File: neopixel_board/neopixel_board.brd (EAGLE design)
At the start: 160 x 100 mm, 63 parts, among them U1 UA7805CKCT, U2 MIC5219, U3 ATMEGA32U4, U4 UA7805CKCT, U5 UA7805CKCT, U6 UA7805CKCT, Y1 16MHz

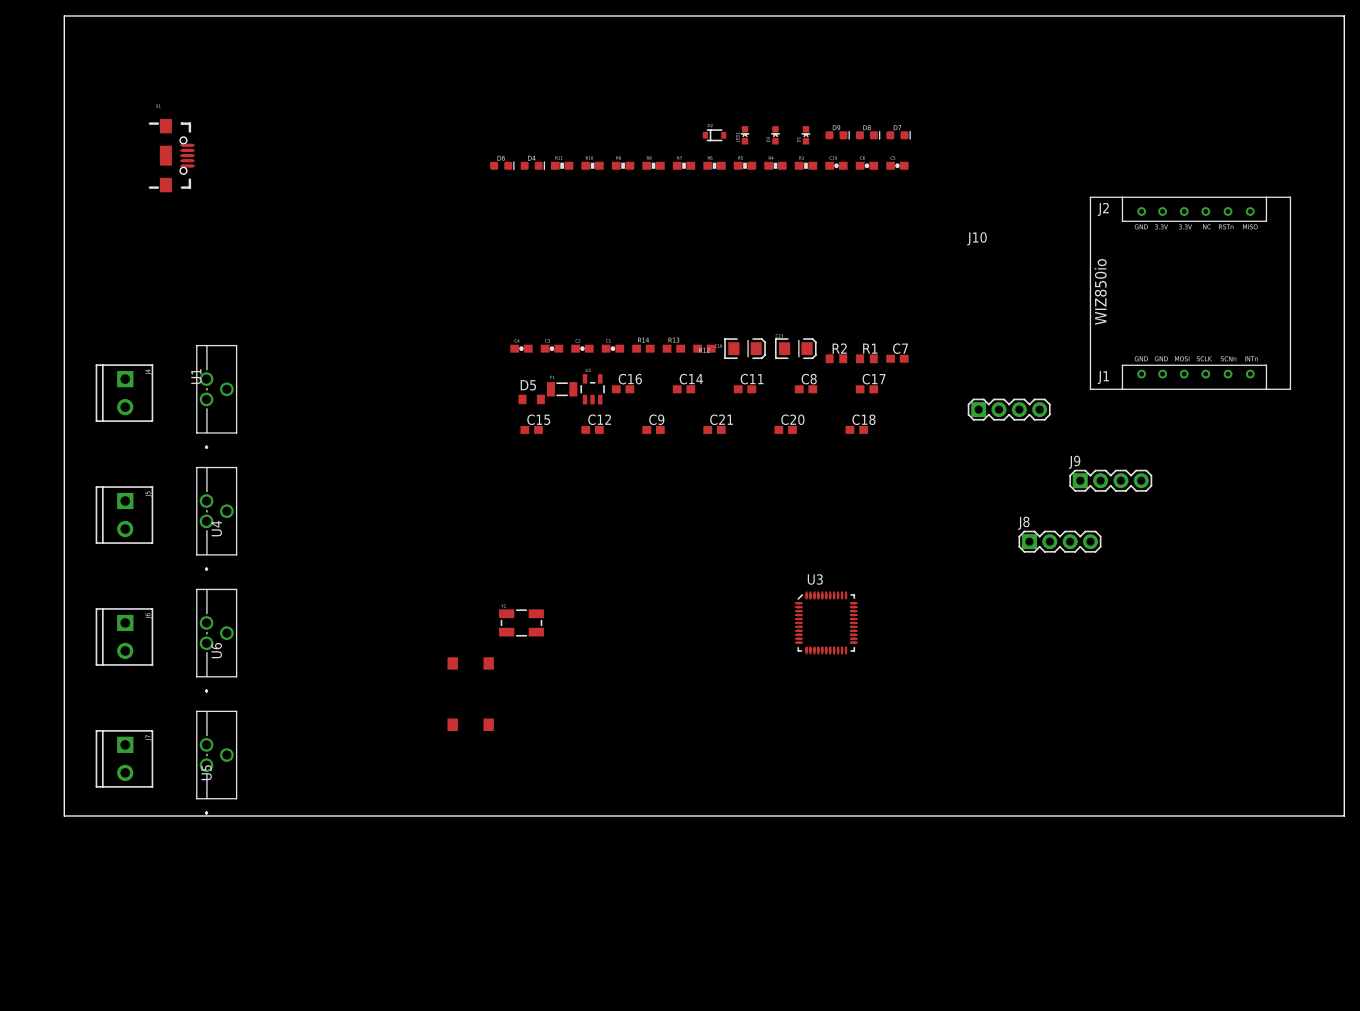
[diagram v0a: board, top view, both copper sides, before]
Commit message: SCH fixes and BRD WIP
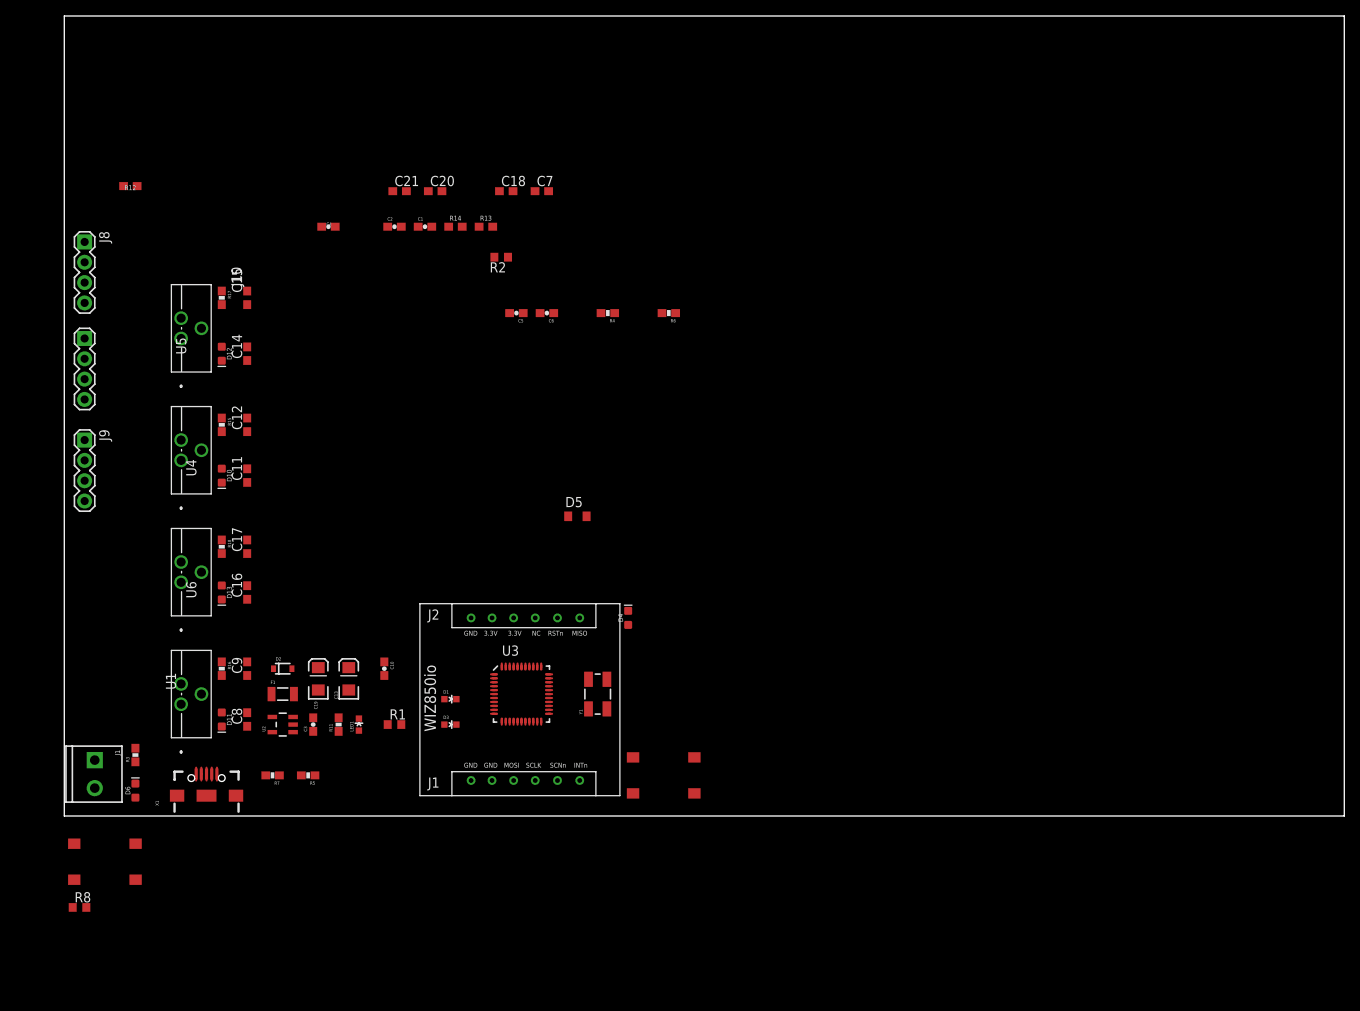
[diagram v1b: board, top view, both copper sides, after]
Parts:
- removed D7, D8, D9: GREEN, SparkFun-LED:LED-0603
- removed J4, J5, J6, J7: (no value), SparkFun-Connectors:SCREWTERMINAL-3.5MM-2
- removed R10, R9: 1K, SparkFun:0603-RES
- added D10, D11, D12, D13: GREEN, SparkFun-LED:LED-0603
- added J1: (no value), SparkFun-Connectors:SCREWTERMINAL-3.5MM-2
- added PB2: PTS645PTS645_SMD1, Training_Board:PTS645_SMD
- added R15, R16, R17, R18: 1K, SparkFun:0603-RES
- R8: value 1K -> (none); device SparkFun:0603-RES -> rcl:R0603
- moved J9 124.6 mm to (2.54, 47.0), turned to 270 degrees
- moved J8 123.9 mm to (2.54, 71.8), turned to 270 degrees
- moved R8 117.2 mm to (1.91, -11.4)
- moved J10 112.1 mm to (2.54, 59.7), turned to 270 degrees
- moved R3 111.6 mm to (8.89, 7.62), turned to 90 degrees
- moved ETH1 98.0 mm to (44.5, 2.54)
- moved R5 93.7 mm to (30.5, 5.08), turned to 180 degrees
- moved R7 91.9 mm to (26.0, 5.08), turned to 180 degrees
- moved D6 90.5 mm to (8.89, 3.17), turned to 90 degrees
- moved LED1 88.1 mm to (36.8, 11.4)
- moved D2 85.8 mm to (27.3, 18.4)
- moved C10 84.5 mm to (40.0, 18.4), turned to 270 degrees
- moved D3 84.1 mm to (48.3, 11.4), turned to 270 degrees
- moved D1 83.3 mm to (48.3, 14.6), turned to 270 degrees
- moved C8 81.1 mm to (22.9, 12.1), turned to 90 degrees
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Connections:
- net MISO renamed ETH_MISO
- net MOSI renamed ETH_MOSI
- removed net A0: U3.36
- removed net A1: U3.37
- removed net A2: U3.38
- removed net A3: U3.39
- removed net A4: U3.40
- removed net A5: U3.41
- removed net D11: U3.12
- removed net D12: U3.26
- removed net D13: U3.32
- removed net D2: U3.19
- removed net D3: U3.18
- removed net D4: U3.25
- removed net D6: U3.27
- removed net D7: U3.1
- removed net D8: U3.28
- removed net N$3: D5.C
- removed net PB5: R13.2
- removed net PB6: R14.2
- removed net PC6: R12.2
- removed net RXI: U3.20
- removed net TXO: U3.21
- removed net VSOURCE1: C8.1, J4.2, R8.2, U1.1
- removed net VSOURCE2: C11.1, J5.2, R3.2, U4.1
- removed net VSOURCE3: C14.1, J6.2, R9.2, U5.1
- removed net VSOURCE4: C16.1, J7.2, R10.2, U6.1
- new net ETH_RST: PB2.P$1, PB2.P$2, R8.2, U3.20
- new net N$21: D6.A, R3.1
- new net VSOURCE: C11.1, C14.1, C16.1, C8.1, J1.2, R3.2, U1.1, U4.1, U5.1, U6.1
- net D10: now also R14.2
- net D5: now also R12.2
- net D9: now also R13.2
- net GND: now also D10.C, D11.C, D12.C, D13.C, J1.1, PB2.P$3, PB2.P$4; no longer D7.C, D8.C, D9.C, J4.1, J5.1, J6.1, J7.1
- net N$10: now also D13.A, R18.2; no longer D7.A, R3.1
- net N$11: now also D11.A, R16.2; no longer D9.A, R10.1
- net N$12: now also D10.A, R15.2; no longer D8.A, R9.1
- net N$13: now also D12.A, R17.2; no longer D6.A, R8.1
- net RAW: now also D5.C
- net VCC1: now also R16.1
- net VCC1_3.3V: now also R8.1
- net VCC2: now also R15.1
- net VCC3: now also R17.1
- net VCC4: now also R18.1

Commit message: SCH finish BRD WIP
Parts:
- removed D13: GREEN, SparkFun-LED:LED-0603
- removed R16: 1K, SparkFun:0603-RES
- added C22: 1000uF, neopixel_board:PCAP_8X10-ELECT
- added XF1: 4.5A, RoboJackets-Fuses:3557-2
- C1, C10, C2, C3, C4, C5, C6: device SparkFun:0603-CAP -> rcl:C0603
- C18: value 1000 uF -> 470 pF
- C20, C21: value 1000 uF -> 1000uF; device rcl:C0603 -> neopixel_board:PCAP_8X10-ELECT
- C7: value (none) -> 0.1uF
- D1: value Yellow -> GREEN; device SparkFun:LED-0603 -> SparkFun-LED:LED-0603
- R1, R2, R8: value (none) -> 1k
- R4: value 330 -> 1K
- moved C18 99.4 mm to (1.91, -5.71)
- moved PB2 82.1 mm to (40.0, 68.6)
- moved R8 82.1 mm to (36.8, 62.9)
- moved R4 50.2 mm to (19.7, 48.9), turned to 270 degrees
- moved C20 39.0 mm to (41.9, 39.4)
- moved D1 31.5 mm to (19.7, 27.9)
- moved R15 30.5 mm to (19.7, 18.4)
- moved C21 29.8 mm to (41.9, 48.3)
- renumbered D10 to D8, D11 to D7, D12 to D9, R17 to R9, R18 to R10
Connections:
- net D10 renamed NEOPIXEL_2
- net D5 renamed NEOPIXEL_0
- net D9 renamed NEOPIXEL_1
- removed net +3.3V: C7.1, ETH1.8, ETH1.9, R2.1
- removed net D14: R4.1, U3.8
- removed net INTN: ETH1.6
- removed net RST: ETH1.11, PB1.P$1, PB1.P$2, R1.2, U3.13
- removed net SCK: U3.9
- removed net SCLK: ETH1.4
- removed net SCNN: ETH1.5
- new net ETH_INT: ETH1.6, U3.27
- new net ETH_SCK: ETH1.4, U3.9
- new net ETH_SCNN: ETH1.5, U3.11
- new net MCU_RST: PB1.P$1, PB1.P$2, R1.2, U3.13
- new net N$16: J1.2, XF1.1, XF1.2
- net AREF: now also C1.1; no longer C1.2
- net ETH_MISO: now also U3.8; no longer U3.11
- net ETH_RST: now also ETH1.11
- net GND: now also C1.2, C22.2, C3.2, C5.2, C6.2, D1.C; no longer C1.1, C3.1, C5.1, C6.1, D13.C
- net N$10: now also D1.A; no longer D13.A
- net N$11: now also R15.2; no longer R16.2
- net N$12: now also R4.2; no longer R15.2
- net N$4: now also C5.1; no longer C5.2
- net N$5: now also C18.1, U2.4; no longer D1.C, R4.2
- net VCC1: now also C6.1, R15.1; no longer C6.2, R16.1
- net VCC1_3.3V: now also C3.1, C7.1, ETH1.8, ETH1.9, R2.1; no longer C3.2, D1.A
- net VCC2: now also C20.1, R4.1; no longer C21.1, R15.1
- net VCC3: now also C21.1; no longer C20.1
- net VCC4: now also C22.1; no longer C18.1
- net VSOURCE: now also XF1.3, XF1.4; no longer J1.2
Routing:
- net VSOURCE: track 0.00 -> 19.5 mm, vias 0 -> 1
- net GND: track 0.00 -> 6.29 mm
- added copper zone on layer 16, net GND
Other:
- board size 160 x 100 mm -> 94 x 86 mm

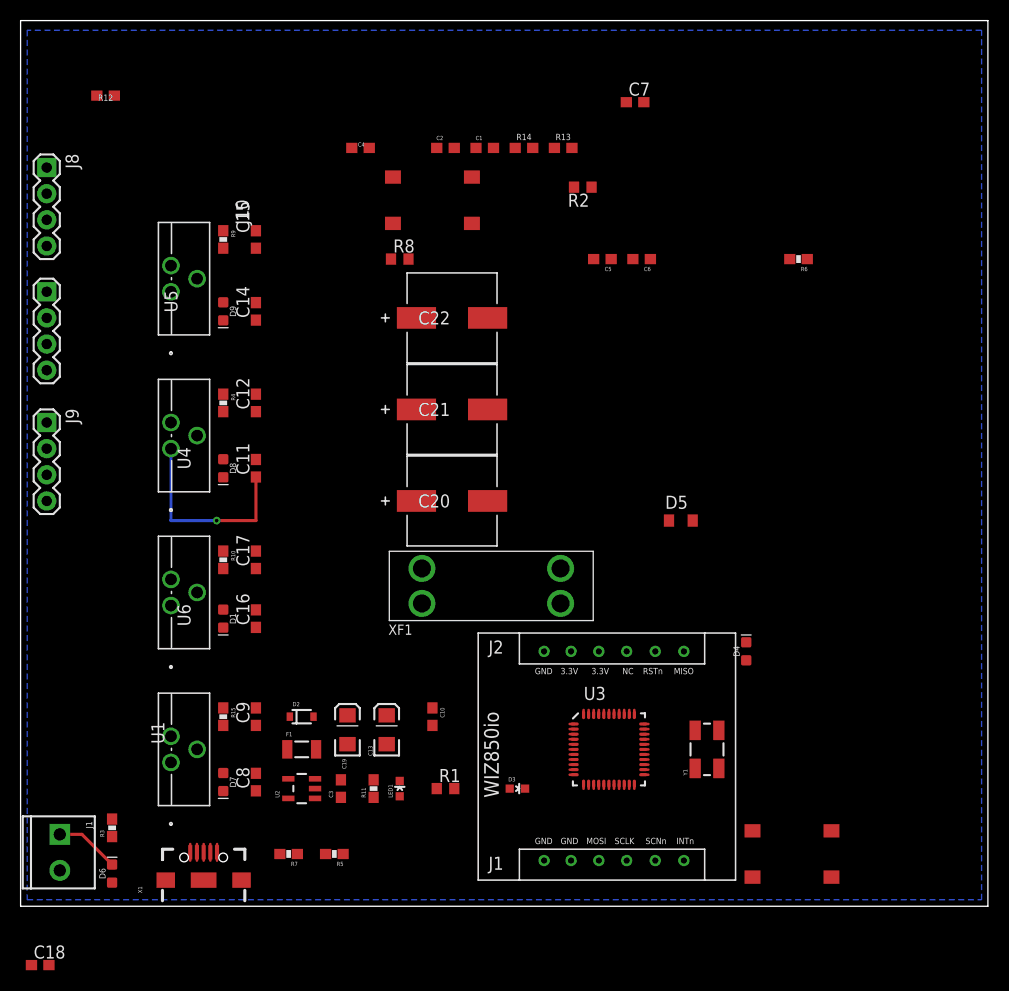
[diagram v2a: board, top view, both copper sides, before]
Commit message: Board WIP
Changed some names and values in schematic. Worked on postioning part on board.
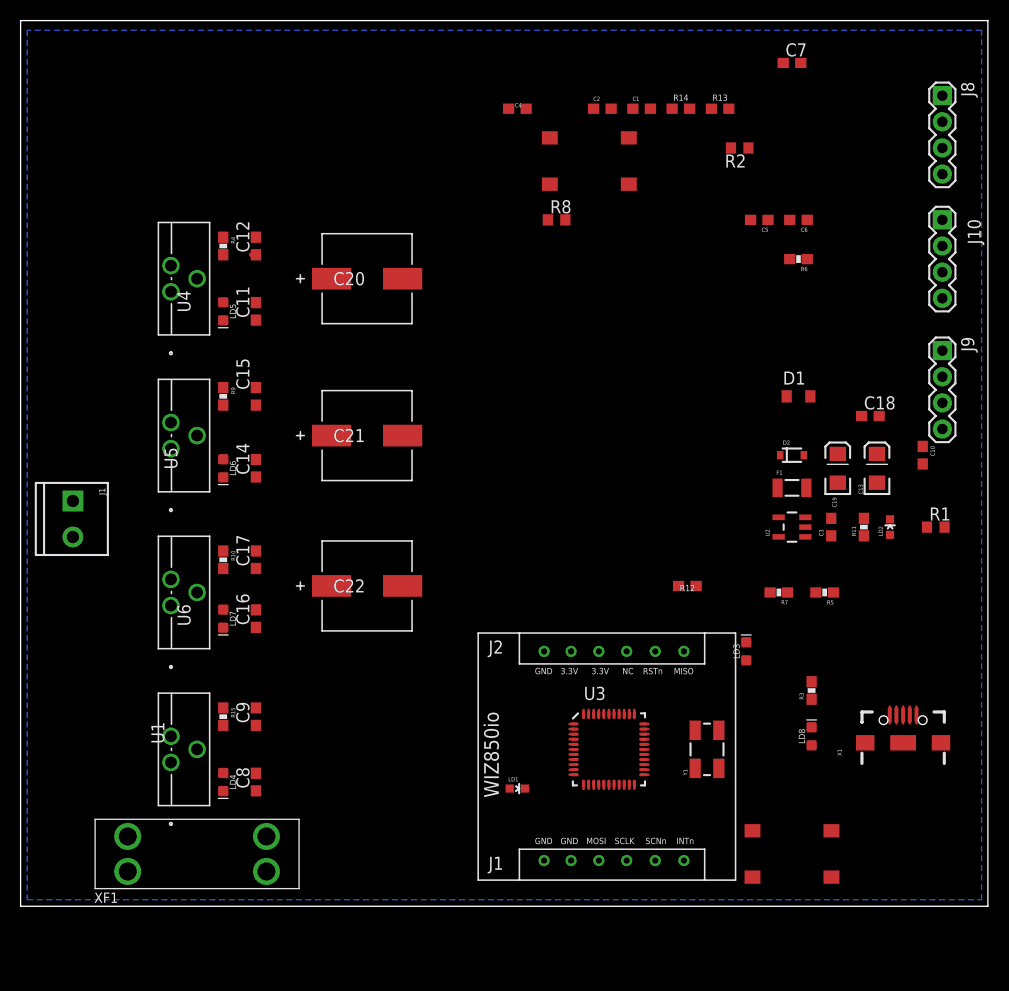
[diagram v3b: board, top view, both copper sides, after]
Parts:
- removed D5: (no value), diode:SOD110-W
- removed D6: GREEN, SparkFun-LED:LED-0603
- removed LED1: Red, SparkFun:LED-0603
- added LD2: RED, SparkFun:LED-0603
- added LD7, LD8: GREEN, SparkFun-LED:LED-0603
- D1: value GREEN -> (none); device SparkFun-LED:LED-0603 -> diode:SOD110-W
- LD1: value Green -> GREEN
- R1, R2, R8: value 1k -> 1kΩ
- R10, R11, R15, R3, R4, R9: value 1K -> 1kΩ
- R12, R13, R14: value 470 -> 470Ω
- R5, R7: value 22 -> 22Ω
- R6: value 330 -> 330Ω
- XF1: value 4.5A -> 4A
- moved C18 96.7 mm to (82.5, 47.6)
- moved J10 87.3 mm to (89.5, 66.7)
- moved J8 87.3 mm to (89.5, 78.7)
- moved J9 87.3 mm to (89.5, 54.0)
- moved R12 73.9 mm to (64.8, 31.1)
- moved R3 69.2 mm to (76.8, 21.0)
- moved X1 69.2 mm to (85.7, 15.9)
- moved D1 59.9 mm to (75.6, 49.5), turned to 0 degrees
- moved D2 54.0 mm to (74.9, 43.8)
- moved F1 54.0 mm to (74.9, 40.6)
- moved R1 54.0 mm to (88.9, 36.8)
- moved R11 54.0 mm to (81.9, 36.8)
- moved U2 54.0 mm to (74.9, 36.8)
- moved C13 54.0 mm to (83.2, 42.5)
- moved C19 54.0 mm to (79.4, 42.5)
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- renumbered D3 to LD1, D4 to LD3, D7 to LD4, D8 to LD6, D9 to LD5
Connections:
- net GND: now also LD2.C, LD7.C, LD8.C; no longer D1.C, D6.C, LED1.C
- net N$10: now also LD7.A; no longer D1.A
- net N$12: now also LD5.A; no longer LD6.A
- net N$13: now also LD6.A; no longer LD5.A
- net N$21: now also LD8.A; no longer D6.A
- net N$38: now also LD2.A; no longer LED1.A
- net RAW: now also D1.C; no longer D5.C
- net UVCC: now also D1.A; no longer D5.A
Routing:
- net VSOURCE: track 19.5 -> 0.00 mm, vias 1 -> 0
- net GND: track 6.29 -> 0.00 mm
